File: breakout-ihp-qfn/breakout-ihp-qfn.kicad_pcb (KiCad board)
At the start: 4 copper layers, 50 x 50 mm, 87 parts, among them J1 Conn_01x12, J2 DF12NB-60DS-0.5V_51, J3 DF12NB-50DS-0.5V_51, U1 AP2112K-1.2, U2 AP2112K-1.8, U3 TT_IHP_ASIC, U4 24LC02

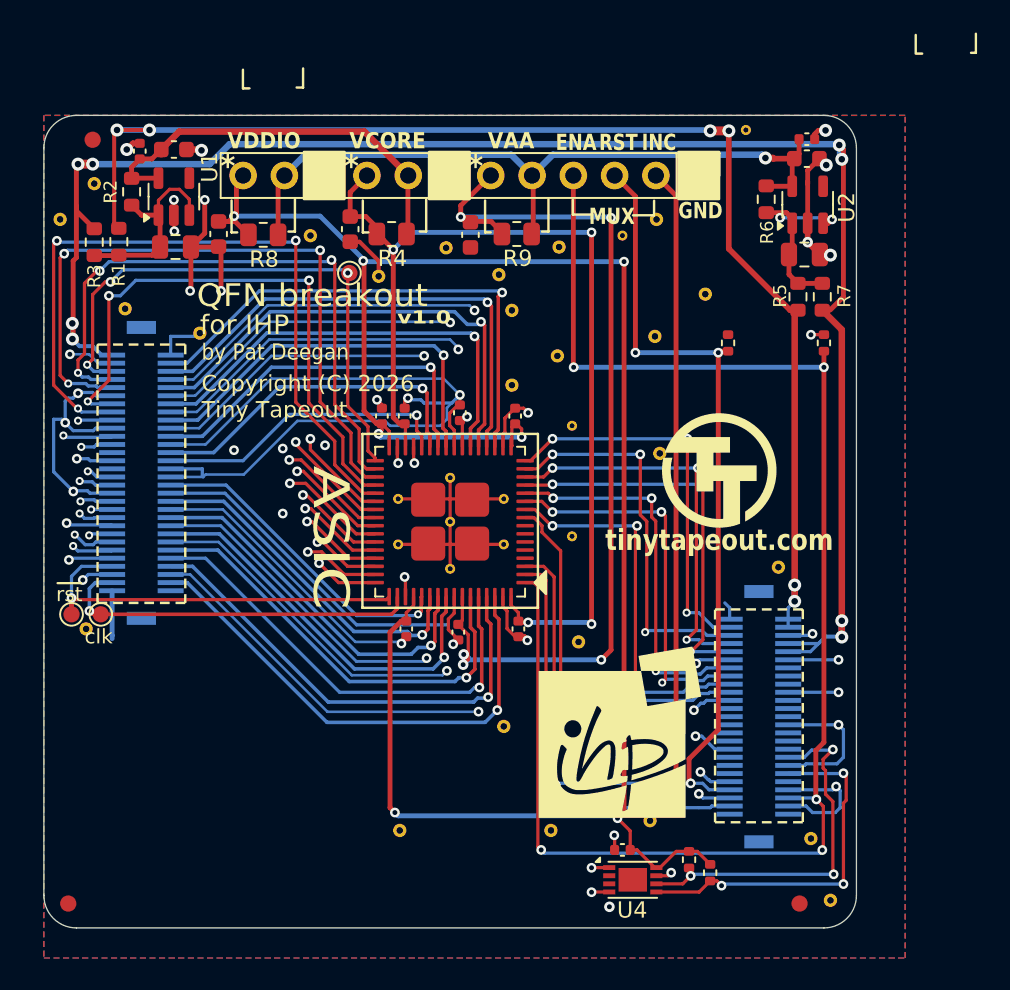
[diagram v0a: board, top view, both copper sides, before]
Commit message: IHP breakout rework from feedback
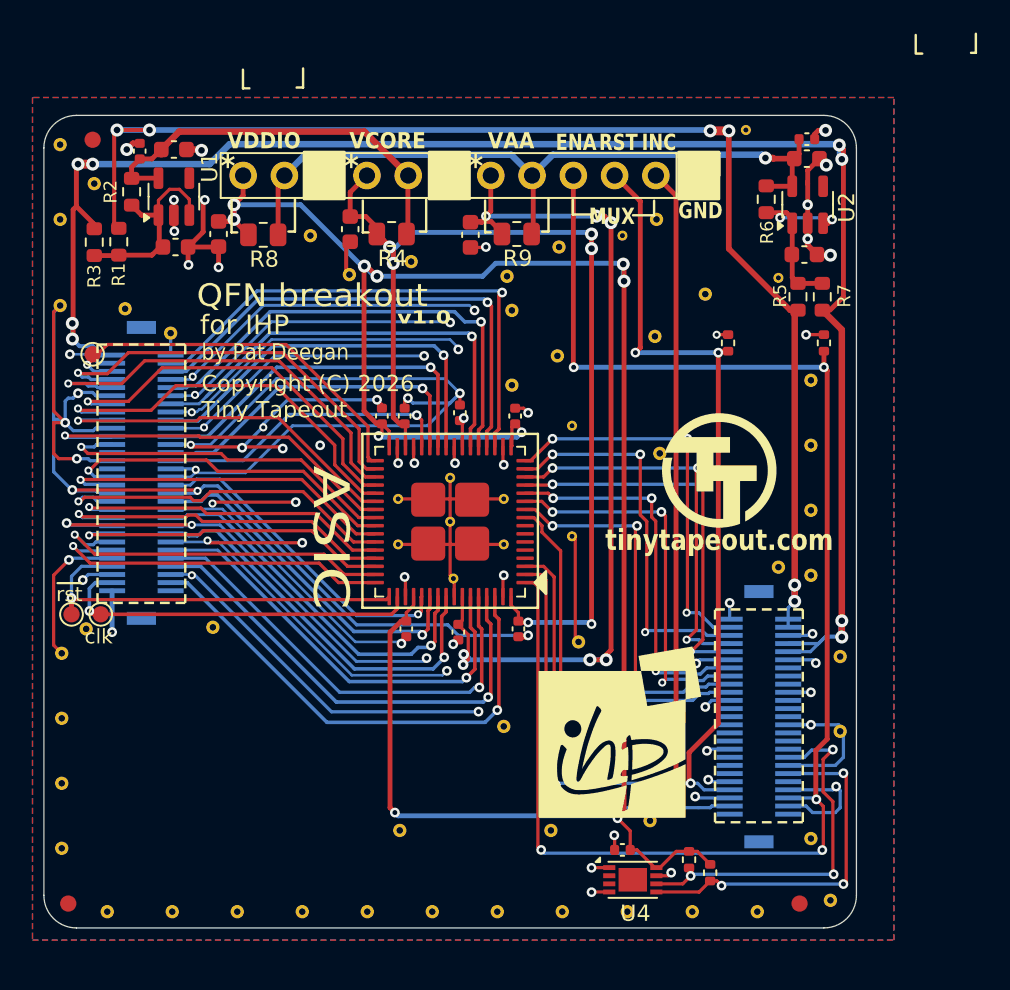
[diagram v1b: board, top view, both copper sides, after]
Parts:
- added STITCH01: StitchingVia-0.4mmDrill, flyingcarsfootprints:StitchingVia-0.4mmDrill, F.Cu at (160.2, 65.3)
- added STITCH01: StitchingVia-0.4mmDrill, flyingcarsfootprints:StitchingVia-0.4mmDrill, F.Cu at (114.0, 50.8)
- added STITCH01: StitchingVia-0.4mmDrill, flyingcarsfootprints:StitchingVia-0.4mmDrill, F.Cu at (123.4, 80.5)
- added STITCH01: StitchingVia-0.4mmDrill, flyingcarsfootprints:StitchingVia-0.4mmDrill, F.Cu at (114.1, 82.1)
- added STITCH10: StitchingVia-0.4mmDrill, flyingcarsfootprints:StitchingVia-0.4mmDrill, F.Cu at (136.9, 98.0)
- added STITCH11: StitchingVia-0.4mmDrill, flyingcarsfootprints:StitchingVia-0.4mmDrill, F.Cu at (140.9, 98.0)
- added STITCH12: StitchingVia-0.4mmDrill, flyingcarsfootprints:StitchingVia-0.4mmDrill, F.Cu at (144.9, 98.0)
- added STITCH13: StitchingVia-0.4mmDrill, flyingcarsfootprints:StitchingVia-0.4mmDrill, F.Cu at (148.9, 98.0)
- added STITCH14: StitchingVia-0.4mmDrill, flyingcarsfootprints:StitchingVia-0.4mmDrill, F.Cu at (152.9, 98.0)
- added STITCH15: StitchingVia-0.4mmDrill, flyingcarsfootprints:StitchingVia-0.4mmDrill, F.Cu at (156.9, 98.0)
- added STITCH16: StitchingVia-0.4mmDrill, flyingcarsfootprints:StitchingVia-0.4mmDrill, F.Cu at (160.2, 69.3)
- added STITCH17: StitchingVia-0.4mmDrill, flyingcarsfootprints:StitchingVia-0.4mmDrill, F.Cu at (160.2, 73.3)
- added STITCH18: StitchingVia-0.4mmDrill, flyingcarsfootprints:StitchingVia-0.4mmDrill, F.Cu at (160.2, 77.3)
- added STITCH18: StitchingVia-0.4mmDrill, flyingcarsfootprints:StitchingVia-0.4mmDrill, F.Cu at (162.0, 86.9)
- added STITCH18: StitchingVia-0.4mmDrill, flyingcarsfootprints:StitchingVia-0.4mmDrill, F.Cu at (162.0, 82.3)
- added STITCH19: StitchingVia-0.4mmDrill, flyingcarsfootprints:StitchingVia-0.4mmDrill, F.Cu at (114.0, 60.7)
- added STITCH2: StitchingVia-0.4mmDrill, flyingcarsfootprints:StitchingVia-0.4mmDrill, F.Cu at (114.1, 86.1)
- added STITCH3: StitchingVia-0.4mmDrill, flyingcarsfootprints:StitchingVia-0.4mmDrill, F.Cu at (114.1, 90.1)
- added STITCH4: StitchingVia-0.4mmDrill, flyingcarsfootprints:StitchingVia-0.4mmDrill, F.Cu at (114.1, 94.1)
- added STITCH5: StitchingVia-0.4mmDrill, flyingcarsfootprints:StitchingVia-0.4mmDrill, F.Cu at (116.9, 98.0)
- added STITCH6: StitchingVia-0.4mmDrill, flyingcarsfootprints:StitchingVia-0.4mmDrill, F.Cu at (120.9, 98.0)
- added STITCH7: StitchingVia-0.4mmDrill, flyingcarsfootprints:StitchingVia-0.4mmDrill, F.Cu at (124.9, 98.0)
- added STITCH8: StitchingVia-0.4mmDrill, flyingcarsfootprints:StitchingVia-0.4mmDrill, F.Cu at (128.9, 98.0)
- added STITCH9: StitchingVia-0.4mmDrill, flyingcarsfootprints:StitchingVia-0.4mmDrill, F.Cu at (132.9, 98.0)
- added STITCHSM01: StitchingVia-0.3mm, flyingcarsfootprints:StitchingVia-0.3mm, F.Cu at (158.2, 59.0)
- C1, C5: footprint Capacitor_SMD:C_0805_2012Metric -> Capacitor_SMD:C_0603_1608Metric
- C2, C4, C6, C8, C9: value 1uF -> 10uF
- moved TP3 16.6 mm to (116.0, 63.7)
- moved STITCH01 2.31 mm to (135.6, 58.0)
- moved STITCH01 1.80 mm to (131.8, 58.8)
- moved STITCH01 1.80 mm to (120.8, 62.4)
- moved STITCHEP01 0.63 mm to (138.2, 77.5)
- moved STITCH01 0.51 mm to (141.5, 58.9)
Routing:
- net GND: track 365.2 -> 427.7 mm, vias 56 -> 76
- net /uio4: track 46.0 -> 24.7 mm, vias 3 -> 1
- net /uio2: track 42.7 -> 26.3 mm, vias 3 -> 1
- net /uio1: track 38.0 -> 25.3 mm, vias 3 -> 1
- net /uio3: track 36.2 -> 24.0 mm, vias 3 -> 1
- net /uio0: track 34.9 -> 24.6 mm, vias 3 -> 1
- net VDD_{IO}: track 126.5 -> 135.8 mm, vias 7 -> 10
- net +5V: track 81.6 -> 89.9 mm
- net +3V3: track 105.4 -> 112.7 mm
- net VDD_{CORE}: track 62.3 -> 68.0 mm, vias 4 -> 6
- net VAA: track 74.4 -> 79.2 mm, vias 6 -> 8
- net /uin0: track 20.7 -> 21.2 mm, vias 2 -> 1
- net /uin2: track 21.8 -> 22.3 mm, vias 2 -> 1
- net /uio5: track 23.0 -> 22.6 mm, vias 2 -> 1
- net /uio6: track 24.3 -> 24.0 mm, vias 2 -> 1
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
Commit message: kinder uo routing
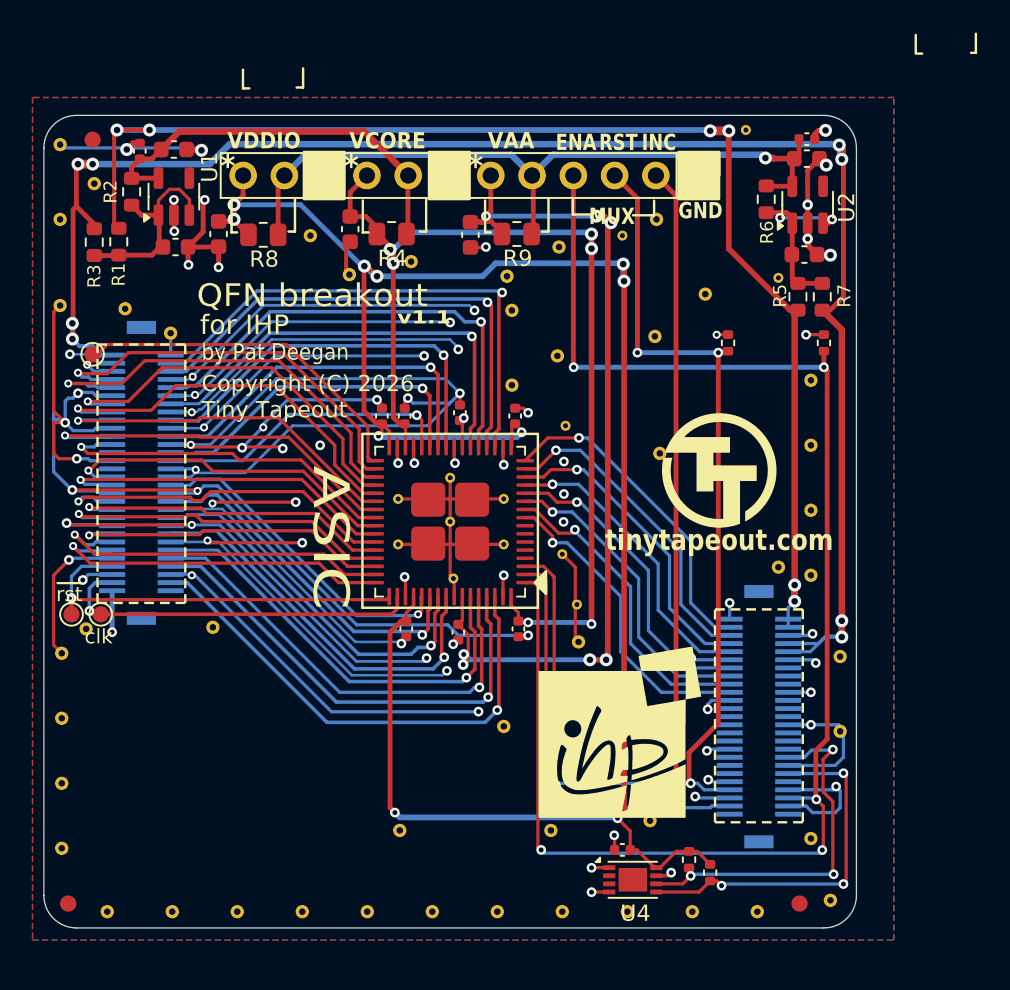
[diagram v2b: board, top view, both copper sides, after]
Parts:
- added STITCHSM01: StitchingVia-0.3mm, flyingcarsfootprints:StitchingVia-0.3mm, F.Cu at (145.8, 79.1)
- moved STITCHSM01 1.25 mm to (144.9, 76.0)
- moved STITCHSM01 0.40 mm to (145.1, 68.1)
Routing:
- net GND: track 427.7 -> 436.0 mm, vias 76 -> 79
- net /uout4: track 24.3 -> 18.5 mm, vias 3 -> 1
- net /uout5: track 24.5 -> 19.1 mm, vias 3 -> 1
- net /uout2: track 23.7 -> 19.1 mm, vias 3 -> 1
- net /uout6: track 24.1 -> 19.7 mm, vias 3 -> 1
- net /uout3: track 23.4 -> 19.2 mm, vias 3 -> 1
- net /uout1: track 23.5 -> 19.3 mm, vias 3 -> 1
- net /uout7: track 24.4 -> 20.2 mm, vias 3 -> 1
- net /uout0: track 22.9 -> 19.3 mm
